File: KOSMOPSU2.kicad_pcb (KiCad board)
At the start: 2 copper layers, 153.7 x 73.9 mm, 28 parts, among them J1 Conn_01x03_Male, J2 Conn_02x05_Odd_Even, J3 Conn_01x03_Male, T1 Myrra 44440 Transformer 240V, U1 L7812, U2 L7912

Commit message: Value Tidy
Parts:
- added G***: LOGO, AA-ROB:GX-F1, F.Cu at (80.5, 79.2)
- F1: value Fuse -> 0.2A 240V
- F2, F3: value Fuse -> 1.5A 240V
- moved R1 3.68 mm to (150.4, 97.4)
- moved R2 2.07 mm to (140.2, 78.0)
- moved G*** 0.36 mm to (161.3, 110.2)

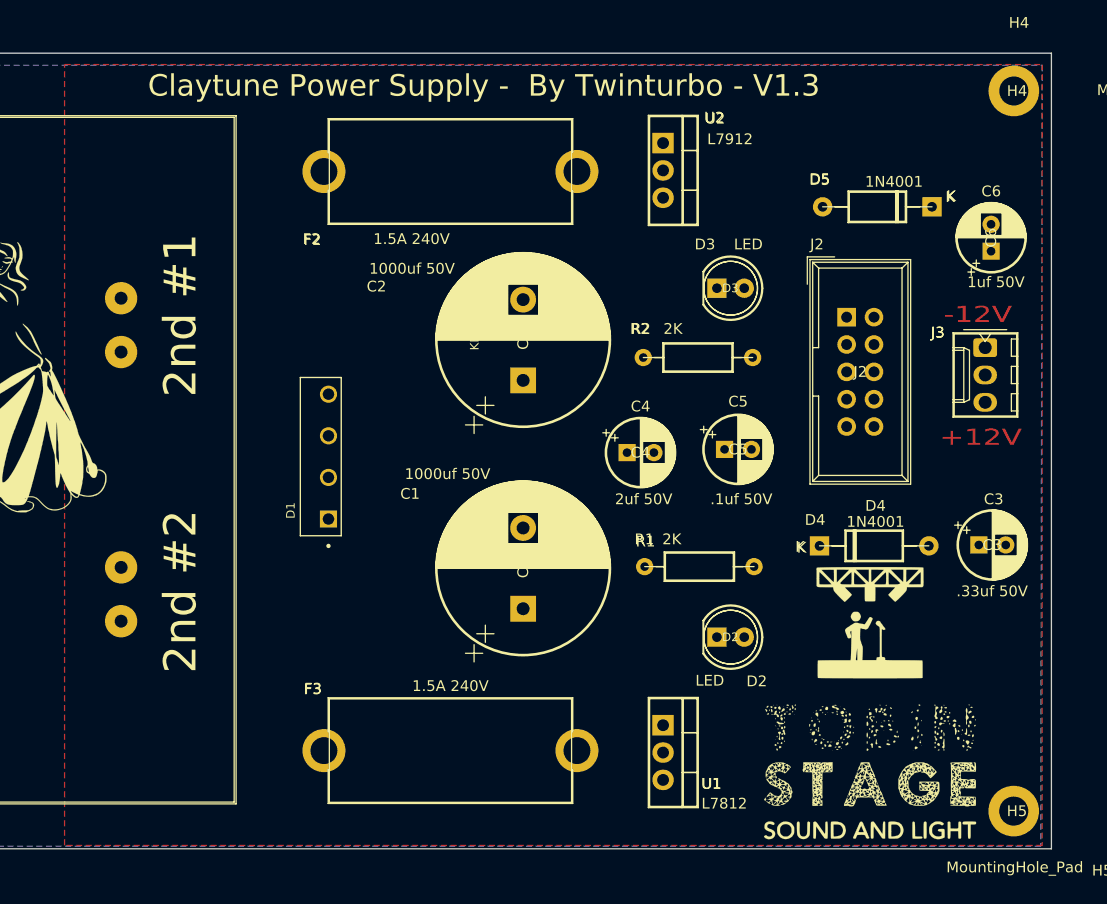
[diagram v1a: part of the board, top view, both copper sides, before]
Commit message: Front Fill removed
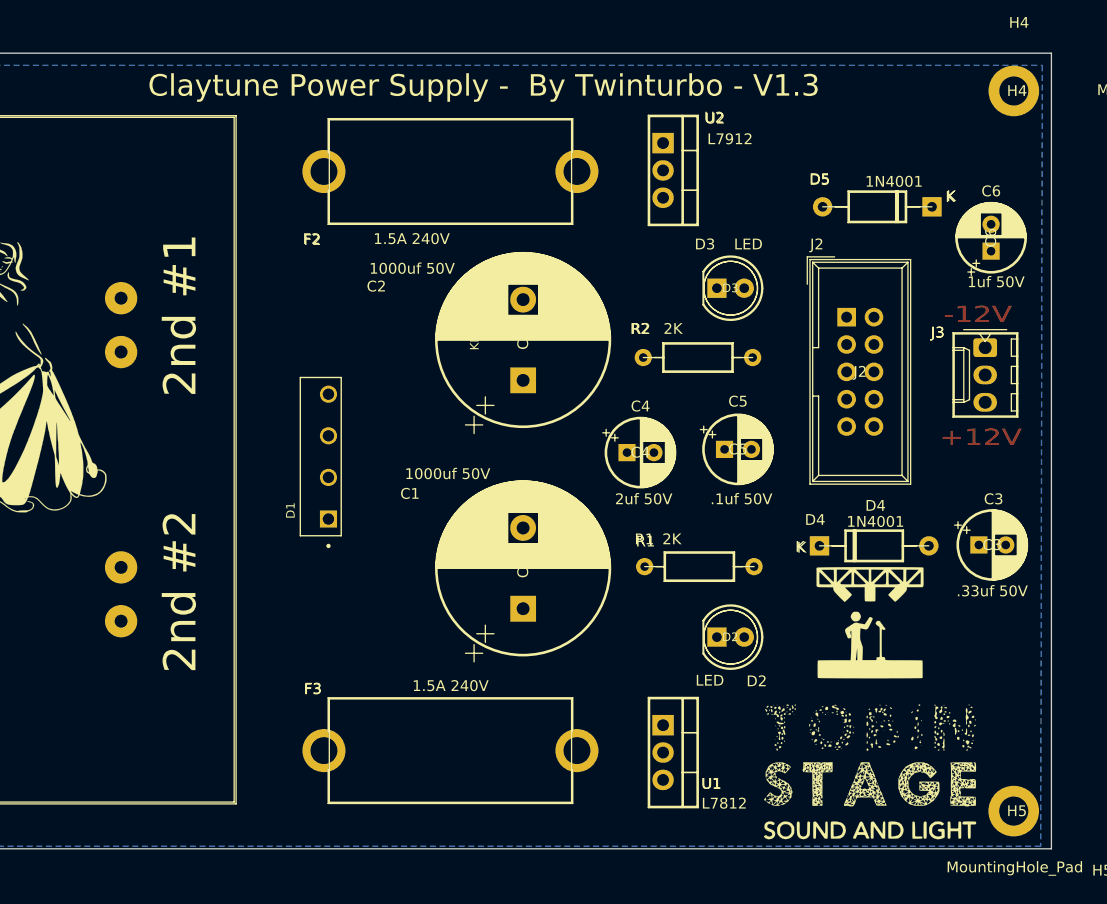
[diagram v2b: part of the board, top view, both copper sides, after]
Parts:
- renumbered G*** to G1, G*** to G2
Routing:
- removed copper zone on F.Cu, net GND
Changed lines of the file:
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@@
   (module AA-ROB:GX-F1 (layer F.Cu)
     (at 80.49 79.22)
-    (fp_text reference G*** (at 0 0) (layer F.SilkS) hide
+    (fp_text reference G2 (at -0.62 -32.59) (layer F.SilkS) hide
       (effects (font (size 1.524 1.524) (thickness 0.3)))
     )
-    (fp_text value LOGO (at 0.75 0) (layer F.SilkS) hide
+    (fp_text value LOGO (at 4.55 -32.54) (layer F.SilkS) hide
       (effects (font (size 1.524 1.524) (thickness 0.3)))
     )
@@
   (module AA-ROB:GX-TOBINLOGO (layer F.Cu)
     (at 161.29 110.16)
-    (fp_text reference G*** (at 0 0) (layer F.SilkS) hide
+    (fp_text reference G1 (at 21.8 -0.21) (layer F.SilkS) hide
       (effects (font (size 1.524 1.524) (thickness 0.3)))
     )
-    (fp_text value LOGO (at 0.75 0) (layer F.SilkS) hide
+    (fp_text value LOGO (at 23.34 2.37) (layer F.SilkS) hide
       (effects (font (size 1.524 1.524) (thickness 0.3)))
     )
@@
   (gr_line (start 178.07 49.68) (end 178.07 123.58) (layer Edge.Cuts) (width 0.05))
   (gr_line (start 24.37 49.68) (end 178.07 49.68) (layer Edge.Cuts) (width 0.05))
-  (zone (net 10) (net_name GND) (layer F.Cu) (hatch edge 0.508)
-    (connect_pads (clearance 0.508))
-    (min_thickness 0.254)
-    (fill (arc_segments 32) (thermal_gap 0.508) (thermal_bridge_width 0.508))
-    (polygon
-      (pts
-        (xy 177.21 123.27) (xy 86.41 123.27) (xy 86.41 50.74) (xy 177.21 50.74)
-      )
-    )
-  )
   (zone (net 10) (net_name GND) (layer B.Cu) (hatch edge 0.508)
     (connect_pads (clearance 0.508))

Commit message: Route Laid Out Manual
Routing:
- net Earth: track 0.00 -> 478.2 mm
- net GND: track 0.00 -> 262.8 mm
- net +12V: track 0.00 -> 82.0 mm
- net Net-(C1-Pad1): track 0.00 -> 70.6 mm
- net Net-(C2-Pad2): track 0.00 -> 60.5 mm
- net -12V: track 0.00 -> 58.1 mm
- net LINE: track 0.00 -> 28.1 mm
- net Net-(F1-Pad1): track 0.00 -> 27.0 mm
- net NEUT: track 0.00 -> 26.4 mm
- net Net-(D1-Pad2): track 0.00 -> 24.8 mm
- net Net-(D1-Pad1): track 0.00 -> 24.6 mm
- net Net-(D1-Pad3): track 0.00 -> 24.6 mm
- net Net-(D1-Pad4): track 0.00 -> 23.2 mm
- net Net-(D2-Pad2): track 0.00 -> 13.8 mm
- net Net-(D3-Pad2): track 0.00 -> 6.70 mm
- removed copper zone on B.Cu, net GND

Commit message: autosync
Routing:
- net GND: track 262.8 -> 264.7 mm
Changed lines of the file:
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@@
     (thickness 1.6)
     (drawings 16)
-    (tracks 197)
+    (tracks 199)
     (zones 0)
     (modules 29)
@@
   (segment (start 91.66 97.44) (end 91.66 77.44) (width 0.5) (layer B.Cu) (net 10))
   (segment (start 129 93.78) (end 129 80.07) (width 0.5) (layer B.Cu) (net 10))
-  (segment (start 129 80.07) (end 140.16 77.95) (width 0.5) (layer F.Cu) (net 10))
   (segment (start 161.59 76.74) (end 159.05 76.74) (width 0.5) (layer F.Cu) (net 10))
   (segment (start 161.59 79.28) (end 161.59 76.74) (width 0.5) (layer B.Cu) (net 10))
@@
   (segment (start 173.99 80.04) (end 173.52 79.57) (width 0.5) (layer B.Cu) (net 10))
   (segment (start 173.99 80.518) (end 173.99 80.04) (width 0.5) (layer B.Cu) (net 10))
+  (segment (start 136.576 81.534) (end 140.16 77.95) (width 0.5) (layer F.Cu) (net 10))
+  (segment (start 129 80.07) (end 130.464 81.534) (width 0.5) (layer F.Cu) (net 10))
+  (segment (start 130.464 81.534) (end 136.576 81.534) (width 0.5) (layer F.Cu) (net 10))
   (segment (start 160.4199 74.2011) (end 160.4136 74.2) (width 0.5) (layer F.Cu) (net 11))
   (segment (start 159.05 74.2) (end 160.4136 74.2) (width 0.5) (layer F.Cu) (net 11))

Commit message: PCB V0.1.4
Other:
- board text added: "Claytune Power Supply - By Twinturbo - V1.4"
- board text removed: "Claytune Power Supply - By Twinturbo - V1.3"
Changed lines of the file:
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@@
     (35 F.Paste user)
     (36 B.SilkS user)
-    (37 F.SilkS user hide)
+    (37 F.SilkS user)
     (38 B.Mask user)
     (39 F.Mask user)
@@
     (effects (font (size 1.5 2) (thickness 0.3)))
   )
-  (gr_text "Claytune Power Supply -  By Twinturbo - V1.3" (at 125.36 52.7) (layer F.SilkS)
+  (gr_text "Claytune Power Supply -  By Twinturbo - V1.4" (at 125.36 52.7) (layer F.SilkS)
     (effects (font (size 2 2) (thickness 0.3)))
   )

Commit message: Transformer Text
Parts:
- added ?: , , F.Cu at (51.6, 82.8)
- added ?: , , F.Cu at (175.3, 7.87)
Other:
- board text added: "Myrra 44452 Transformer 115V"
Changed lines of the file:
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@@
   (general
     (thickness 1.6)
-    (drawings 16)
+    (drawings 17)
     (tracks 199)
     (zones 0)
-    (modules 29)
+    (modules 31)
     (nets 16)
   )
@@
     (add_net GND)
   )
+  (module "" (layer F.Cu)
+    (at 51.562 82.804)
+    (fp_text reference "" (at 175.26 7.874) (layer F.SilkS)
+      (effects (font (size 1.27 1.27) (thickness 0.15)))
+    )
+    (fp_text value "" (at 175.26 7.874) (layer F.SilkS)
+      (effects (font (size 1.27 1.27) (thickness 0.15)))
+    )
+    (fp_text user "Myrra 44440 Transformer 240V " (at 223.012 21.336) (layer F.SilkS)
+      (effects (font (size 3 2) (thickness 0.15)))
+    )
+  )
+  (module "" (layer F.Cu)
+    (at 175.26 7.874)
+    (fp_text reference "" (at 80.49 79.22) (layer F.SilkS)
+      (effects (font (size 1.27 1.27) (thickness 0.15)))
+    )
+    (fp_text value "" (at 80.49 79.22) (layer F.SilkS)
+      (effects (font (size 1.27 1.27) (thickness 0.15)))
+    )
+    (fp_text user "Myrra 44440 Transformer 240V " (at 118.844 97.254) (layer F.SilkS)
+      (effects (font (size 3 2) (thickness 0.15)))
+    )
+  )
   (module AA-ROB:GX-F1 (layer F.Cu)
     (at 80.49 79.22)
@@
       (effects (font (size 1 1) (thickness 0.15)))
     )
-    (fp_text value "Myrra 44440 Transformer 240V " (at 32.45 4.42 90) (layer F.SilkS)
+    (fp_text value "Myrra 44440 Transformer 240V " (at 32.372 2.14 90) (layer F.SilkS)
       (effects (font (size 3 2) (thickness 0.15)))
     )
@@
     )
   )
-  (gr_text "DANGER LIVE MAINS" (at 48.85 88.64 90) (layer F.SilkS)
+  (gr_text "Myrra 44452 Transformer 115V " (at 54.864 86.868 90) (layer F.SilkS)
+    (effects (font (size 3 2) (thickness 0.15)))
+  )
+  (gr_text "DANGER LIVE MAINS" (at 46.99 88.64 90) (layer F.SilkS)
     (effects (font (size 2 2) (thickness 0.5)))
   )

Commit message: Cap Update
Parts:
- C3: value .33uf 50V -> .1uf 50V
- C4: value 2uf 50V -> .2uf 50V
- C6: value 1uf 50V -> .1uf 50V
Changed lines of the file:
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@@
-(kicad_pcb (version 20171130) (host pcbnew "(5.1.7)-1")
+(kicad_pcb (version 20171130) (host pcbnew 5.1.5-52549c5~86~ubuntu18.04.1)
   (general
     (thickness 1.6)
@@
       (effects (font (size 1 1) (thickness 0.15)))
     )
-    (fp_text value "1uf 50V" (at -2.878 0.454 180) (layer F.SilkS)
+    (fp_text value ".1uf 50V" (at -2.878 0.454 180) (layer F.SilkS)
       (effects (font (size 1 1) (thickness 0.15)))
     )
@@
       (effects (font (size 1 1) (thickness 0.15)))
     )
-    (fp_text value "2uf 50V" (at 1.55 4.33) (layer F.SilkS)
+    (fp_text value ".2uf 50V" (at 1.55 4.33) (layer F.SilkS)
       (effects (font (size 1 1) (thickness 0.15)))
     )
@@
       (effects (font (size 1 1) (thickness 0.15)))
     )
-    (fp_text value ".33uf 50V" (at 1.23 4.3) (layer F.SilkS)
+    (fp_text value ".1uf 50V" (at 1.23 4.3) (layer F.SilkS)
       (effects (font (size 1 1) (thickness 0.15)))
     )
